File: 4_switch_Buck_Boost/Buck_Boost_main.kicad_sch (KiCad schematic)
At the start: 12 parts, among them J1 Screw_Terminal_2x5.08, J2 Screw_Terminal_2x5.08, J3 Screw_Terminal_2x2.54, Q1 CSD18532Q5B, Q2 CSD18532Q5B, Q3 CSD18532Q5B, Q4 CSD18532Q5B, U1 LT8390EUFD_PBF

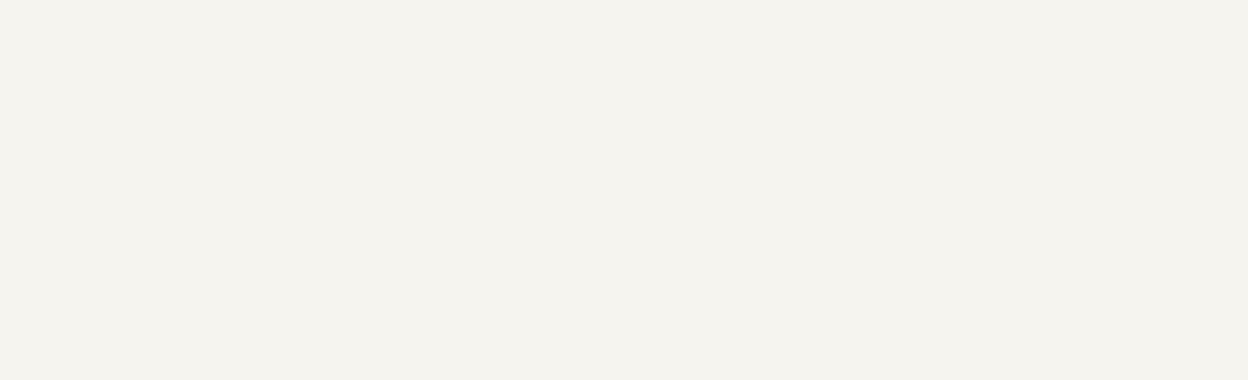
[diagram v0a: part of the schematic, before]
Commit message: Updated KiCad schematic with selected caps and resistors; saved snapshot to History
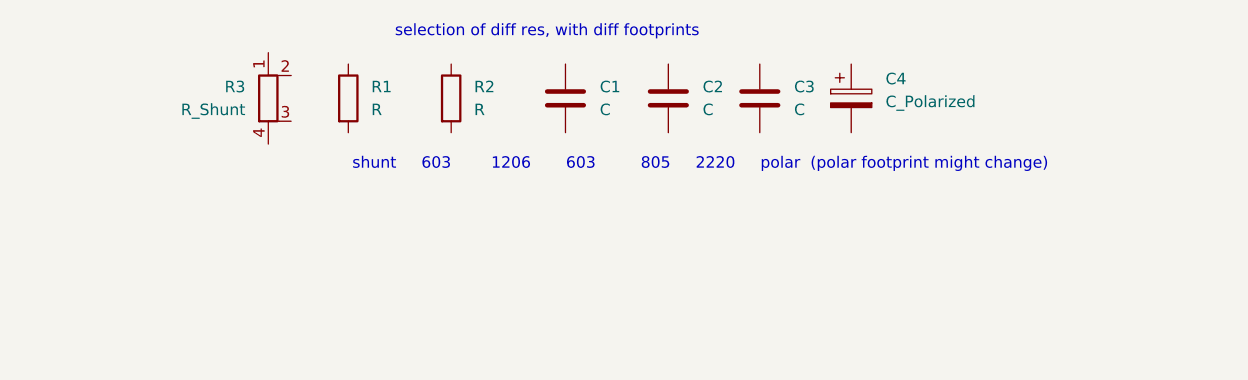
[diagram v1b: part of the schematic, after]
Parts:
- added C1: C, rsx_capacitors:C_0603_1608Metric, symbol Device:C
- added C2: C, rsx_capacitors:C_0805_2012Metric, symbol Device:C
- added C3: C, rsx_capacitors:C_2220_5750Metric_Pad1.97x5.40mm_HandSolder, symbol Device:C
- added C4: C_Polarized, Capacitor_SMD:CP_Elec_8x10.5, symbol Device:C_Polarized
- added R1: R, rsx_resistors:R_0603_1608Metric, symbol Device:R
- added R2: R, rsx_resistors:R_1206_3216Metric, symbol Device:R
- added R3: R_Shunt, Resistor_SMD:R_Shunt_Vishay_WSK2512_6332Metric_T1.19mm, symbol Device:R_Shunt
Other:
- note added: "selection of diff res, with diff footprints"
- note added: "shunt 603 1206 603 805 2220 polar (polar footprint might change)"

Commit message: main pwr path
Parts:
- added C101, C102: 2.5u, rsx_capacitors:C_0603_1608Metric, symbol Device:C
- added R101: 5m, Resistor_SMD:R_Shunt_Vishay_WSK2512_6332Metric_T1.19mm, symbol Device:R_Shunt
- added R102: 10m, Resistor_SMD:R_Shunt_Vishay_WSK2512_6332Metric_T1.19mm, symbol Device:R_Shunt
- added R103: 232k, rsx_resistors:R_0603_1608Metric, symbol Device:R
- added R104: 10k, rsx_resistors:R_0603_1608Metric, symbol Device:R
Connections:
- net GND: now also Q3.1 (S), Q3.2 (S), Q3.3 (S), Q4.1 (S), Q4.2 (S), Q4.3 (S), U1.29 (GND), R104.2
- net Vout: now also F2.2
- net at L1.1: now also R101.1
- net at L1.2: now also Q2.5 (D), Q4.5 (D), U1.23 (SW2), C102.2
- net at Q3.4 (G): now also U1.26 (BG1)
- net at Q3.5 (D): now also Q1.1 (S), Q1.2 (S), Q1.3 (S), U1.28 (SW1), C101.1, R101.4
- net at Q2.1 (S), Q2.2 (S), Q2.3 (S): now also U1.21 (VOUT), R102.4
- net at Q2.4 (G): now also U1.22 (TG2)
- net at Q4.4 (G): now also U1.25 (BG2)
- net at F2.1: now also R102.1, R103.1
- net at Q1.4 (G): now also U1.1 (TG1)
- net at U1.11 (ISP): now also R102.3
- net at U1.12 (ISN): now also R102.2
- net at U1.16 (FB): now also R103.2, R104.1
- net at U1.2 (LSP): now also R101.3
- net at U1.24 (BST2): now also C102.1
- net at U1.27 (BST1): now also C101.2
- net at U1.3 (LSN): now also R101.2
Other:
- moved on the sheet: F2, L1, Q1, Q2, Q3, Q4, U1

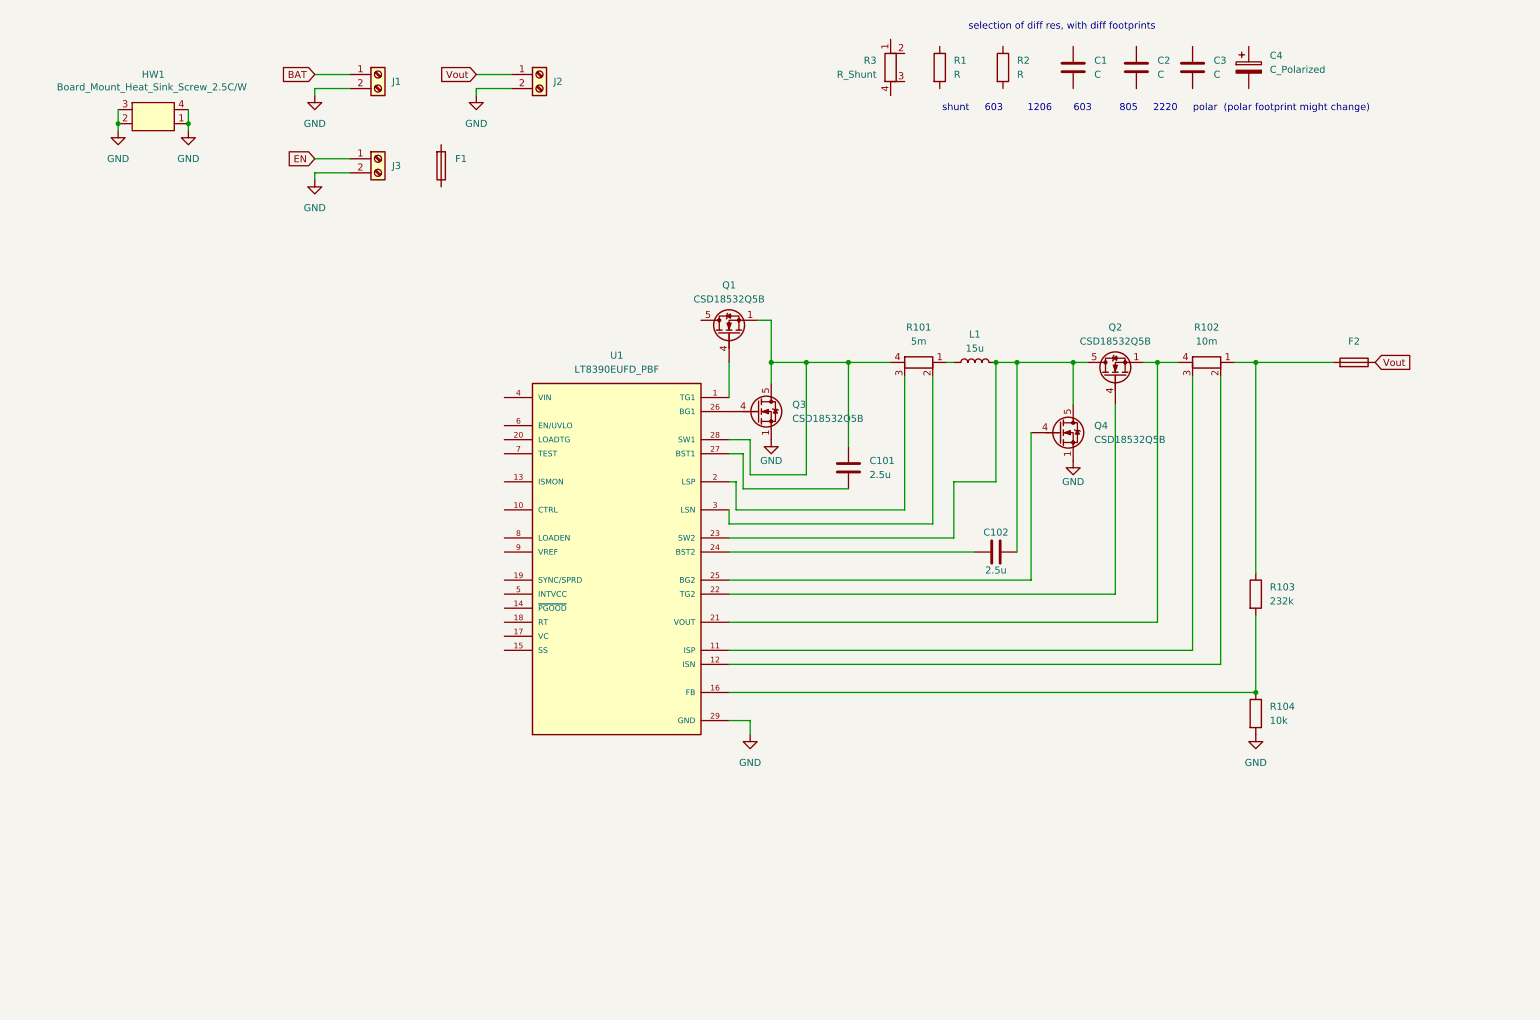
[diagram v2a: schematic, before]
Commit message: Reformat to be human readable
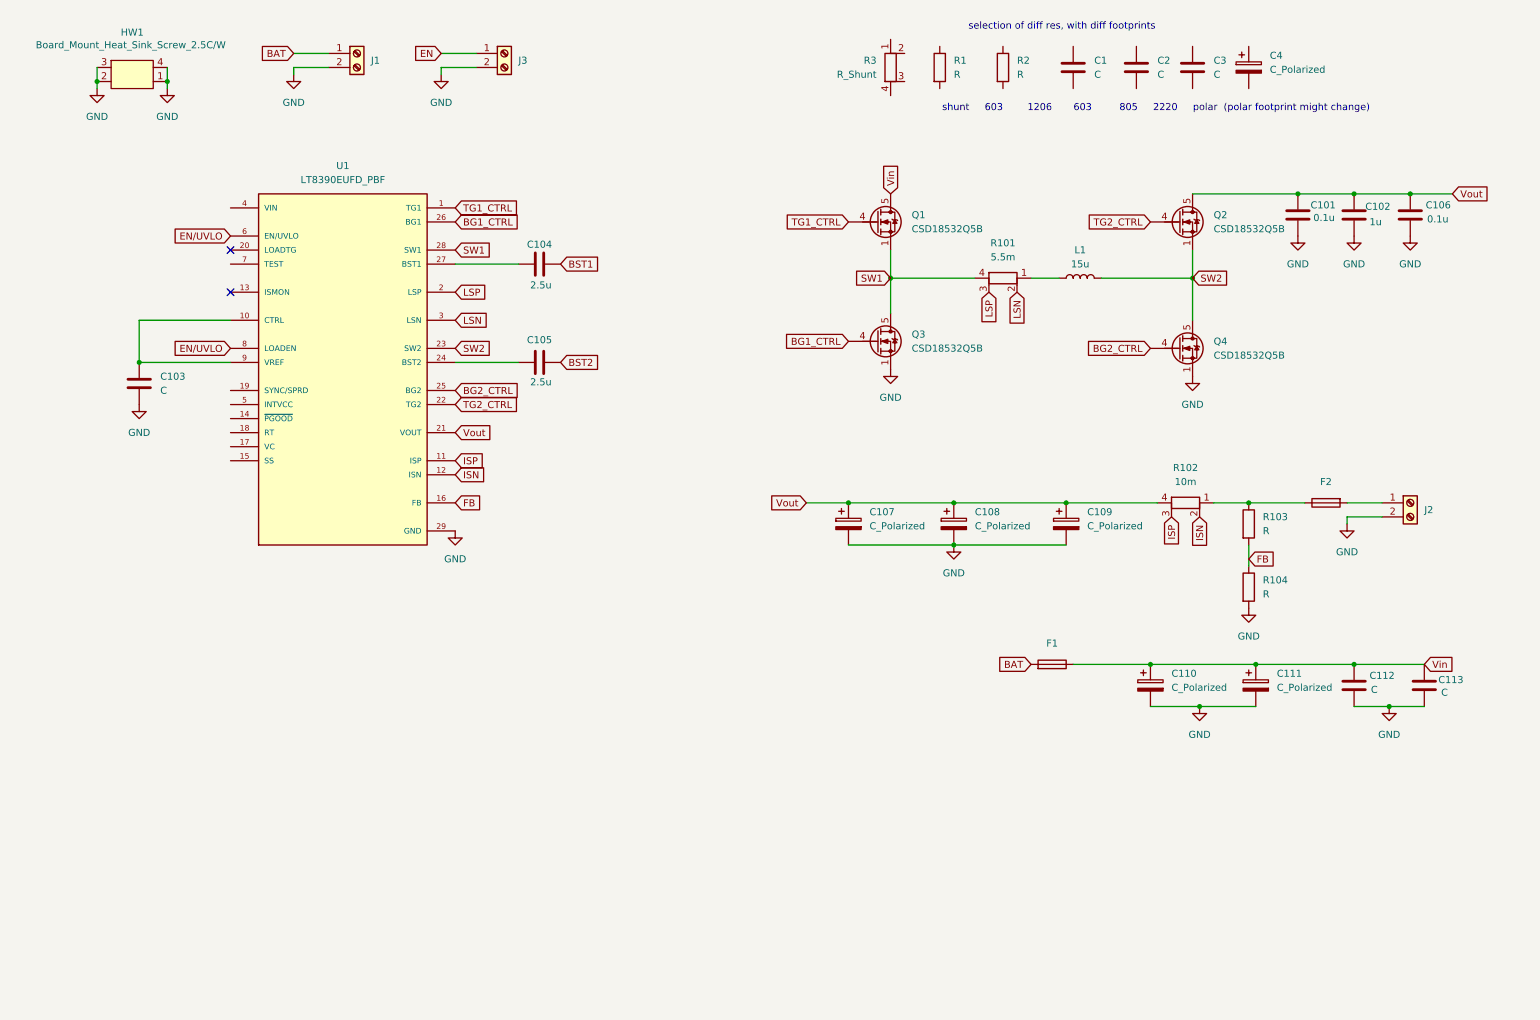
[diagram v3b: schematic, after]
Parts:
- added C103, C112, C113: C, rsx_capacitors:C_0603_1608Metric, symbol Device:C
- added C104, C105: 2.5u, rsx_capacitors:C_0603_1608Metric, symbol Device:C
- added C106: 0.1u, rsx_capacitors:C_0603_1608Metric, symbol Device:C
- added C107, C108, C109, C110, C111: C_Polarized, Capacitor_SMD:CP_Elec_8x10.5, symbol Device:C_Polarized
- C101: value 2.5u -> 0.1u
- C102: value 2.5u -> 1u
- R101: value 5m -> 5.5m
- R103: value 232k -> R
- R104: value 10k -> R
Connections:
- net BAT: now also F1.1
- net GND: now also C101.2, C102.2, C103.2, C106.2, C107.2, C108.2, C109.2, C110.2, C111.2, C112.2, C113.2
- net Vout: now also C101.1, C102.1, Q2.5 (D), R102.4, U1.21 (VOUT), C106.1, C107.1, C108.1, C109.1; no longer F2.2, J2.1 (Pin_1)
- net FB: now reaches R103.2, R104.1, U1.16 (FB)
- net at R102.1, R103.1: now also F2.2; no longer F2.1
- net ISN: now reaches R102.2, U1.12 (ISN)
- net ISP: now reaches R102.3, U1.11 (ISP)
- net SW2: now reaches Q2.1 (S), Q2.2 (S), Q2.3 (S)
- net SW2: now also L1.2, Q4.5 (D), U1.23 (SW2); no longer R102.4, U1.21 (VOUT)
- net BG1_CTRL: now reaches Q3.4 (G), U1.26 (BG1)
- net SW1: now reaches Q1.1 (S), Q1.2 (S), Q1.3 (S), Q3.5 (D), R101.4, U1.28 (SW1)
- net SW1: no longer C101.1
- net at U1.24 (BST2): now also C105.1; no longer C102.1
- net at U1.27 (BST1): now also C104.1; no longer C101.2
- net TG2_CTRL: now reaches Q2.4 (G), U1.22 (TG2)
- net BG2_CTRL: now reaches Q4.4 (G), U1.25 (BG2)
- net TG1_CTRL: now reaches Q1.4 (G), U1.1 (TG1)
- net Vin: now reaches Q1.5 (D)
- net Vin: now also F1.2, C110.1, C111.1, C112.1, C113.1
- net LSN: now reaches R101.2, U1.3 (LSN)
- net LSP: now reaches R101.3, U1.2 (LSP)
- net at U1.10 (CTRL): now also U1.9 (VREF), C103.1
- net EN/UVLO: now reaches U1.6 (EN/UVLO)
- net EN/UVLO: now also U1.8 (LOADEN)
- new net: F2.1, J2.1 (Pin_1)
- new net BST1: C104.2
- new net BST2: C105.2
- no-connect marks 0 -> 2
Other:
- moved on the sheet: F1, F2, HW1, J1, J2, J3, L1, Q1, Q2, Q3, Q4, R101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

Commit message: High side switch
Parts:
- added C114, C115, C116: 0.1u, rsx_capacitors:C_0805_2012Metric, symbol Device:C
- added D101: LED_G, rsx_leds:LED_0805_2012Metric, symbol rsx_LEDs:LED_G
- added Q101: 2N7002K, rsx_packages_TO_SOT:SOT-23, symbol rsx_Transistors:2N7002K
- added Q103: BSS83P, Package_TO_SOT_SMD:SOT-23, symbol Transistor_FET:BSS83P
- added R105, R106: 100K, rsx_resistors:R_0603_1608Metric, symbol Device:R
- added R107, R109: 10K, rsx_resistors:R_0603_1608Metric, symbol Device:R
- added R108: 4K, rsx_resistors:R_0603_1608Metric, symbol Device:R
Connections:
- net EN/UVLO: now also C115.1, Q103.3 (D), R107.1
- net GND: now also C114.2, C115.2, C116.2, Q101.2 (S), R107.2, R108.2, R109.2
- net Vin: now also C116.1, Q103.2 (S), R106.1
- net EN renamed ENABLE
- net ENABLE: now also C114.1, D101.2 (A), Q101.1 (G), R109.1
- new net: Q101.3 (D), R105.2
- new net: Q103.1 (G), R105.1, R106.2
- new net: D101.1 (K), R108.1

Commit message: Adding filtering capacitance values
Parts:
- added C117: 4.7n, rsx_capacitors:C_0603_1608Metric, symbol Device:C
- added C118: 22n, rsx_capacitors:C_0603_1608Metric, symbol Device:C
- added C119: 100p, rsx_capacitors:C_0603_1608Metric, symbol Device:C
- added C120: C, rsx_capacitors:C_0603_1608Metric, symbol Device:C
- added R110: R, rsx_resistors:R_0603_1608Metric, symbol Device:R
- C103: value C -> 4.7uF
- C107, C108: value C_Polarized -> 33u
- C109, C110, C111: value C_Polarized -> 22u
- C112: value C -> 4.7n
- C113: value C -> 22n
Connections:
- net SW1 is gone; now on net BST1: Q1.1 (S), Q1.2 (S), Q1.3 (S), Q3.5 (D), R101.4, U1.28 (SW1)
- net SW2 is gone; now on net BST2: L1.2, Q2.1 (S), Q2.2 (S), Q2.3 (S), Q4.5 (D), U1.23 (SW2)
- net GND: now also U1.7 (TEST), C117.2, C118.2, C119.2, C120.2
- net Vin: now also C109.1, U1.4 (VIN)
- net Vout: now also C117.1, C118.1; no longer C109.1
- net Vc: now reaches U1.17 (VC)
- net Vc: now also C119.1, R110.1
- new net: C120.1, R110.2
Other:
- moved on the sheet: C107, C108, C110, C111, F1, Q1, Q3

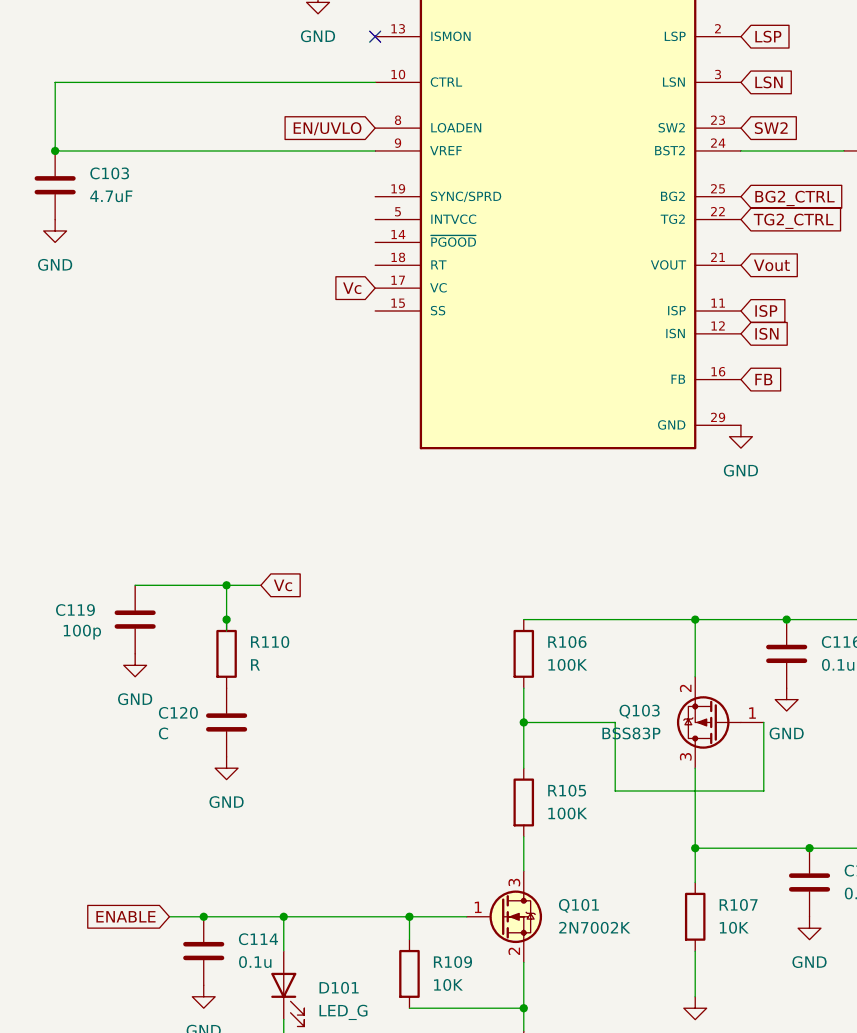
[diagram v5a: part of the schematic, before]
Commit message: LT8390 pins
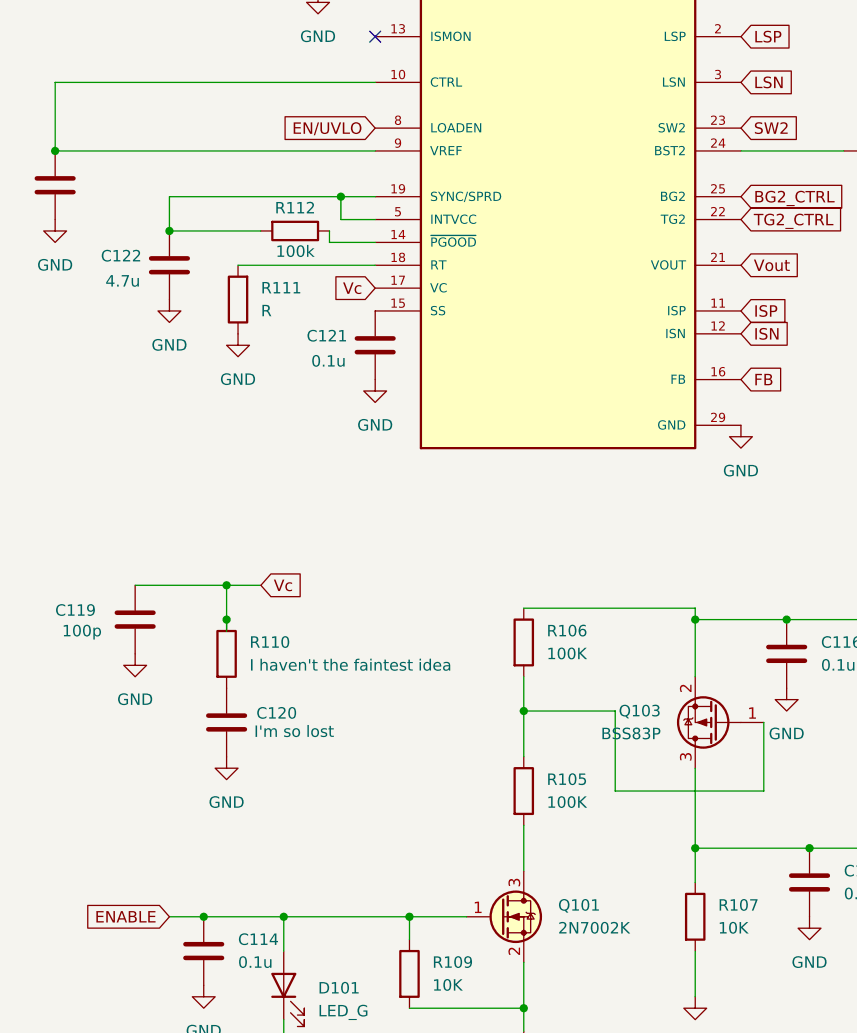
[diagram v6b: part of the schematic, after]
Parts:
- added C121: 0.1u, rsx_capacitors:C_0603_1608Metric, symbol Device:C
- added C122: 4.7u, rsx_capacitors:C_0603_1608Metric, symbol Device:C
- added R111: R, rsx_resistors:R_0603_1608Metric, symbol Device:R
- added R112: 100k, rsx_resistors:R_0603_1608Metric, symbol Device:R
- C120: value C -> I'm so lost
- R110: value R -> I haven't the faintest idea
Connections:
- net GND: now also C121.2, C122.2, R111.1
- net at U1.14 (~{PGOOD}): now also R112.1
- net at U1.15 (SS): now also C121.1
- net at U1.18 (RT): now also R111.2
- net at U1.19 (SYNC/SPRD): now also U1.5 (INTVCC), C122.1, R112.2
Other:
- moved on the sheet: R105, R106

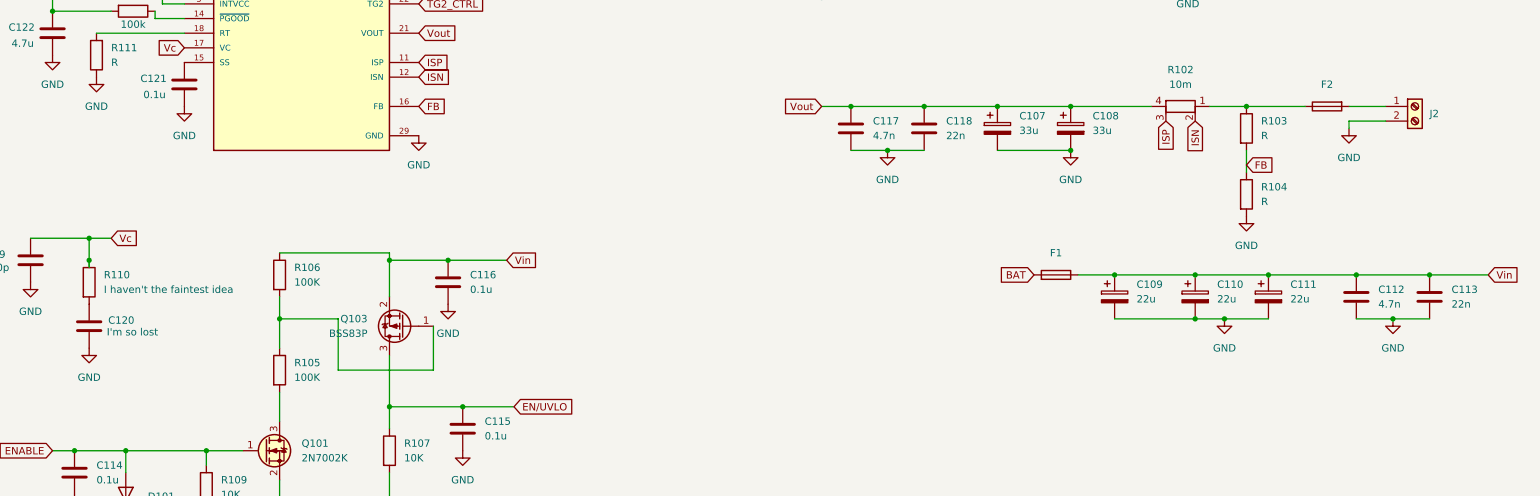
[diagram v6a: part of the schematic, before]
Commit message: Update buck boost feedback circuit, add trimmer and decoupling caps
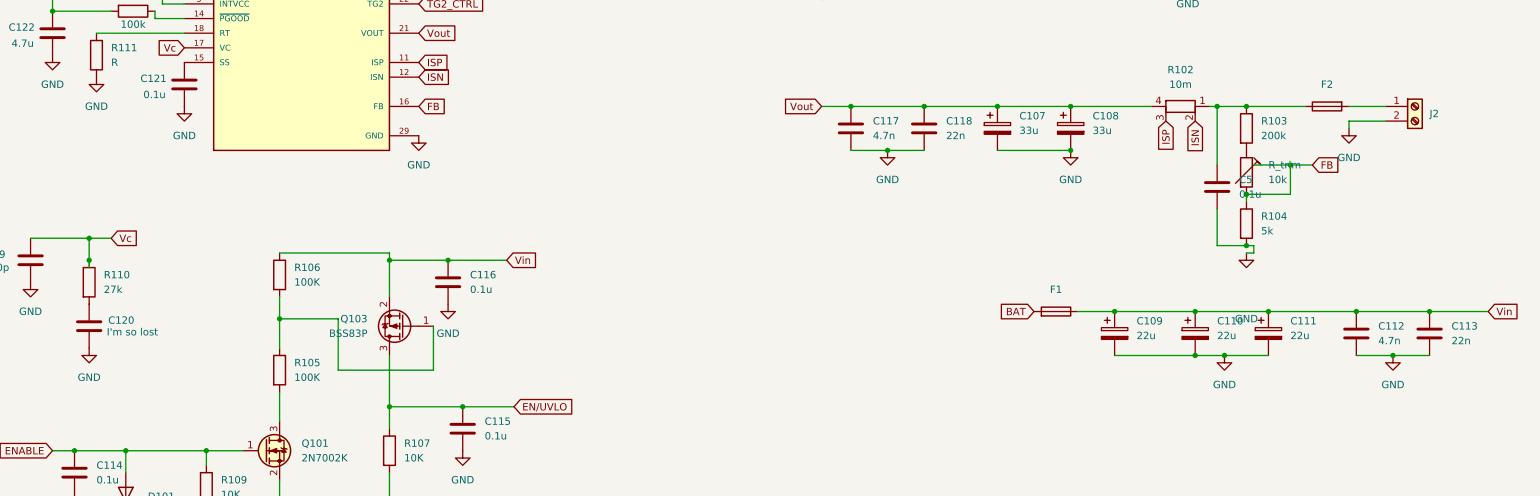
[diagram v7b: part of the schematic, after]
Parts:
- added C5: 0.1u, symbol Device:C
- added R_trim: 10k, symbol Device:R_Trim
- R103: value R -> 200k
- R104: value R -> 5k
- R110: value I haven't the faintest idea -> 27k
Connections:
- net FB: now also R_trim.2; no longer R103.2
- net GND: now also C5.2
- net at F2.2, R102.1, R103.1: now also C5.1
- new net: R103.2, R_trim.1
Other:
- moved on the sheet: C109, C110, C111, C112, C113, F1, R104
